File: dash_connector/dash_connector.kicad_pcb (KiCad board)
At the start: 2 copper layers, 7.6 x 27.3 mm, 2 parts, among them P1 CONN_02X05, U1 AXE610124

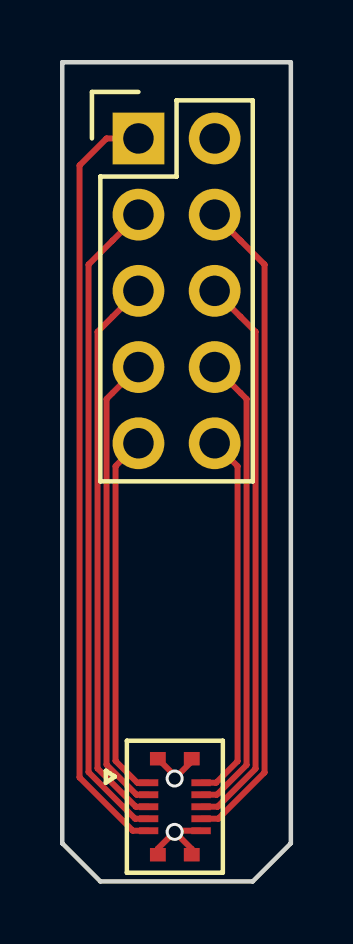
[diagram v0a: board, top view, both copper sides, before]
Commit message: [dash_connector] Fix pinout and add silkscreen.
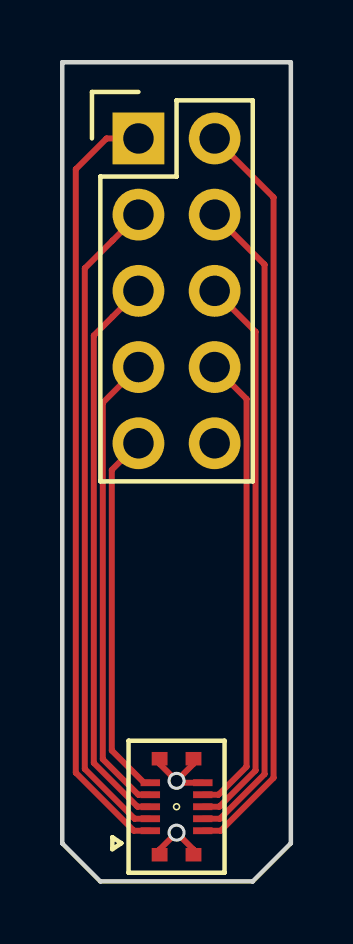
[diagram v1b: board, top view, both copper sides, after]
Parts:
- moved U1 0.06 mm to (148.6, 106.1), turned to 180 degrees
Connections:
- P1 pad 1: Net-(P1-Pad1) -> /VCC
- P1 pad 10: Net-(P1-Pad10) -> GND
- P1 pad 2: GND -> /PB4
- P1 pad 3: Net-(P1-Pad3) -> /JTAG_JTDI
- P1 pad 4: Net-(P1-Pad4) -> /JTAG_SWO
- P1 pad 5: Net-(P1-Pad5) -> /JTAG_SWDIO
- P1 pad 6: Net-(P1-Pad6) -> /DEBUG_RX
- P1 pad 7: Net-(P1-Pad7) -> /JTAG_SWCLK
- P1 pad 8: Net-(P1-Pad8) -> /DEBUG_TX
- P1 pad 9: Net-(P1-Pad9) -> /NC?
- U1 pad 1: Net-(P1-Pad9) -> /VCC
- U1 pad 10: Net-(P1-Pad10) -> GND
- U1 pad 2: Net-(P1-Pad7) -> /PB4
- U1 pad 3: Net-(P1-Pad5) -> /JTAG_JTDI
- U1 pad 4: Net-(P1-Pad3) -> /JTAG_SWO
- U1 pad 5: Net-(P1-Pad1) -> /JTAG_SWDIO
- U1 pad 6: GND -> /DEBUG_RX
- U1 pad 7: Net-(P1-Pad4) -> /JTAG_SWCLK
- U1 pad 8: Net-(P1-Pad6) -> /DEBUG_TX
- U1 pad 9: Net-(P1-Pad8) -> /NC?
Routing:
- net /VCC: track 0.00 -> 25.9 mm
- net Net-(P1-Pad1): track 25.8 -> 0.00 mm
- net /PB4: track 0.00 -> 25.2 mm
- net /JTAG_JTDI: track 0.00 -> 22.1 mm
- net Net-(P1-Pad4): track 22.0 -> 0.00 mm
- net /JTAG_SWO: track 0.00 -> 22.0 mm
- net Net-(P1-Pad3): track 21.9 -> 0.00 mm
- net /JTAG_SWDIO: track 0.00 -> 18.8 mm
- net Net-(P1-Pad6): track 18.8 -> 0.00 mm
- net /DEBUG_RX: track 0.00 -> 18.8 mm
- net Net-(P1-Pad5): track 18.7 -> 0.00 mm
- net /JTAG_SWCLK: track 0.00 -> 15.6 mm
- net Net-(P1-Pad8): track 15.6 -> 0.00 mm
- net /DEBUG_TX: track 0.00 -> 15.6 mm
- net Net-(P1-Pad7): track 15.5 -> 0.00 mm
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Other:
- board text added: "PB4 SWO RX TX GND"
- board text added: "VCC TDI SWDIO SWCLK NC"
